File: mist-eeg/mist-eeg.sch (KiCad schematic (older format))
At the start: 3 parts

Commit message: Hooked-up the SoM
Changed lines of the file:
@@
 Wire Wire Line
 	2450 4200 2550 4200
-Text Label 1600 4200 2    50   ~ 0
-SD_DATA_DAT0
 Text Label 1600 4300 2    50   ~ 0
-SD_DATA_DAT1
+SD_DAT1
 Text Label 1600 4400 2    50   ~ 0
-SD_DATA_DAT2
+SD_DAT2
 Text Label 1600 4500 2    50   ~ 0
-SD_DATA_DAT3
+SD_DAT3
 Text Label 2550 4200 0    50   ~ 0
-SD_DATA_CMD
+SD_CMD
 Text Label 2550 4300 0    50   ~ 0
-SD_DATA_CLK
+SD_CLK
 Text Label 2550 4400 0    50   ~ 0
-SD_DATA_CONNECTED
+~SD_CONNECTED~
 $Sheet
 S 4250 1000 800  600
@@
 F7 "LRCLK" I R 5050 1200 50
 F8 "BCLK" I R 5050 1100 50
-F9 "PWR_OK" I R 5050 1450 50
+F9 "PWR_OK" I L 4250 1500 50
+F10 "MCLK" I R 5050 1400 50
 $EndSheet
 $Sheet
@@
 	4450 3700 4550 3700
 Text Label 4450 3400 2    50   ~ 0
-SD_DATA_DAT0
+SD_DAT0
 Text Label 4450 3500 2    50   ~ 0
-SD_DATA_DAT1
+SD_DAT1
 Text Label 4450 3600 2    50   ~ 0
-SD_DATA_DAT2
+SD_DAT2
 Text Label 4450 3700 2    50   ~ 0
-SD_DATA_DAT3
+SD_DAT3
 Wire Wire Line
 	4450 4000 4550 4000
@@
 	4550 3800 4450 3800
 Text Label 4450 3800 2    50   ~ 0
-SD_DATA_CMD
+SD_CMD
 Text Label 4450 3900 2    50   ~ 0
-SD_DATA_CLK
+SD_CLK
 Text Label 4450 4000 2    50   ~ 0
-SD_DATA_CONNECTED
+~SD_CONNECTED~
 Text Label 6500 3500 0    50   ~ 0
 USER1_G
@@
 Text Label 6500 4550 0    50   ~ 0
 USER
-Text Label 4500 4200 2    50   ~ 0
+Text Label 4500 4300 2    50   ~ 0
 ~EEG_CS~
-Text Label 4500 4300 2    50   ~ 0
+Text Label 4500 4400 2    50   ~ 0
 EEG_MOSI
-Text Label 4500 4400 2    50   ~ 0
+Text Label 4500 4500 2    50   ~ 0
 EEG_MISO
 Wire Wire Line
-	4500 4400 4550 4400
-Wire Wire Line
-	4550 4300 4500 4300
-Wire Wire Line
-	4500 4200 4550 4200
-Text Label 4500 4500 2    50   ~ 0
+	4500 4500 4550 4500
+Wire Wire Line
+	4550 4400 4500 4400
+Wire Wire Line
+	4500 4300 4550 4300
+Text Label 4500 4600 2    50   ~ 0
 EEG_SCK
 Wire Wire Line
-	4500 4500 4550 4500
-Wire Wire Line
 	4500 4600 4550 4600
-Text Label 4500 4600 2    50   ~ 0
+Wire Wire Line
+	4500 4700 4550 4700
+Text Label 4500 4700 2    50   ~ 0
 ~EEG_PWDN~
-Text Label 4500 4700 2    50   ~ 0
+Text Label 4500 4800 2    50   ~ 0
 ~EEG_RESET~
 Wire Wire Line
-	4500 4700 4550 4700
-Wire Wire Line
 	4500 4800 4550 4800
-Text Label 4500 4800 2    50   ~ 0
+Wire Wire Line
+	4500 4900 4550 4900
+Text Label 4500 4900 2    50   ~ 0
 EEG_START
-Text Label 4500 4900 2    50   ~ 0
+Text Label 4500 5000 2    50   ~ 0
 ~EEG_DRDY~
 Wire Wire Line
-	4500 4900 4550 4900
+	4500 5000 4550 5000
 Text Label 6500 4900 0    50   ~ 0
 AUDIO_BCLK
@@
 Text Label 1450 1250 2    50   ~ 0
 +5V0_ANA
-Text Label 4500 5100 2    50   ~ 0
+Text Label 4500 5150 2    50   ~ 0
 CTRL_SDA
-Text Label 4500 5200 2    50   ~ 0
+Text Label 4500 5250 2    50   ~ 0
 CTRL_SCL
 Wire Wire Line
-	4500 5200 4550 5200
-Wire Wire Line
-	4550 5100 4500 5100
+	4500 5250 4550 5250
+Wire Wire Line
+	4550 5150 4500 5150
 Text Label 2500 1350 0    50   ~ 0
 CTRL_SDA
@@
 Wire Wire Line
 	1450 1450 1500 1450
-Text Label 2550 4500 0    50   ~ 0
+Text Label 1600 4650 2    50   ~ 0
 +3V3_SD
 Wire Wire Line
-	2450 4500 2550 4500
+	1700 4650 1600 4650
 $Sheet
-S 1700 4150 750  450
+S 1700 4150 750  550
 U 60A0E6BC
 F0 "SD_DATA" 50
@@
 F6 "DAT0" B L 1700 4200 50
 F7 "DAT1" B L 1700 4300 50
-F8 "CON" O R 2450 4400 50
-F9 "+PWR_IN" I R 2450 4500 50
+F8 "~CD~" O R 2450 4400 50
+F9 "+PWR_IN" I L 1700 4650 50
+F10 "~RST~" I R 2450 4500 50
 $EndSheet
 Wire Wire Line
@@
 Wire Wire Line
 	2500 1550 2450 1550
-Text Label 4500 5350 2    50   ~ 0
+Text Label 4500 5400 2    50   ~ 0
 +5V_SOM
 Wire Wire Line
-	4500 5350 4550 5350
-Text Label 5100 1450 0    50   ~ 0
+	4500 5400 4550 5400
+Text Label 4200 1500 2    50   ~ 0
 AUDIO_PWR_OK
 Wire Wire Line
-	5100 1450 5050 1450
+	4200 1500 4250 1500
 $Sheet
 S 4550 3200 1900 2300
@@
 F0 "SoM" 50
 F1 "Coral-SoM.sch" 50
-F2 "SD_DATA_DAT0" B L 4550 3400 50
-F3 "SD_DATA_DAT1" B L 4550 3500 50
-F4 "SD_DATA_DAT2" B L 4550 3600 50
-F5 "SD_DATA_DAT3" B L 4550 3700 50
-F6 "SD_DATA_CMD" O L 4550 3800 50
-F7 "SD_DATA_CLK" O L 4550 3900 50
-F8 "SD_DATA_CONNECTED" I L 4550 4000 50
+F2 "SD_DAT0" B L 4550 3400 50
+F3 "SD_DAT1" B L 4550 3500 50
+F4 "SD_DAT2" B L 4550 3600 50
+F5 "SD_DAT3" B L 4550 3700 50
+F6 "SD_CMD" O L 4550 3800 50
+F7 "SD_CLK" O L 4550 3900 50
+F8 "~SD_CONNECTED~" I L 4550 4000 50
 F9 "USER1_R" O R 6450 3400 50
 F10 "USER1_G" O R 6450 3500 50
@@
 F19 "USER" I R 6450 4550 50
 F20 "START" I R 6450 4650 50
-F21 "~EEG_CS~" O L 4550 4200 50
-F22 "EEG_MOSI" O L 4550 4300 50
-F23 "EEG_MISO" I L 4550 4400 50
-F24 "EEG_SCK" O L 4550 4500 50
-F25 "~EEG_PWDN~" O L 4550 4600 50
-F26 "~EEG_RESET~" O L 4550 4700 50
-F27 "EEG_START" O L 4550 4800 50
-F28 "~EEG_DRDY~" I L 4550 4900 50
+F21 "~EEG_CS~" O L 4550 4300 50
+F22 "EEG_MOSI" O L 4550 4400 50
+F23 "EEG_MISO" I L 4550 4500 50
+F24 "EEG_SCK" O L 4550 4600 50
+F25 "~EEG_PWDN~" O L 4550 4700 50
+F26 "~EEG_RESET~" O L 4550 4800 50
+F27 "EEG_START" O L 4550 4900 50
+F28 "~EEG_DRDY~" I L 4550 5000 50
 F29 "AUDIO_BCLK" O R 6450 4900 50
 F30 "AUDIO_LRCLK" O R 6450 5000 50
@@
 F33 "AUDIO_SDA" B R 6450 5300 50
 F34 "AUDIO_SCL" O R 6450 5400 50
-F35 "CTRL_SDA" B L 4550 5100 50
-F36 "CTRL_SCL" O L 4550 5200 50
-F37 "+5V_SOM" I L 4550 5350 50
+F35 "CTRL_SDA" B L 4550 5150 50
+F36 "CTRL_SCL" O L 4550 5250 50
+F37 "+5V_SOM" I L 4550 5400 50
+F38 "+3V3_IN" I L 4550 3300 50
+F39 "AUDIO_MCLK" O R 6450 4800 50
+F40 "~SD_RST~" O L 4550 4100 50
 $EndSheet
+Text Label 5100 1400 0    50   ~ 0
+AUDIO_MCLK
+Wire Wire Line
+	5100 1400 5050 1400
+Text Label 6500 4800 0    50   ~ 0
+AUDIO_MCLK
+Wire Wire Line
+	6500 4800 6450 4800
+Text Label 4450 3300 2    50   ~ 0
++3V3_SD
+Wire Wire Line
+	4450 3300 4550 3300
+Text Label 1600 4200 2    50   ~ 0
+SD_DAT0
+Text Label 2550 4500 0    50   ~ 0
+~SD_RST~
+Wire Wire Line
+	4450 4100 4550 4100
+Text Label 4450 4100 2    50   ~ 0
+~SD_RST~
+Wire Wire Line
+	2450 4500 2550 4500
 $EndSCHEMATC

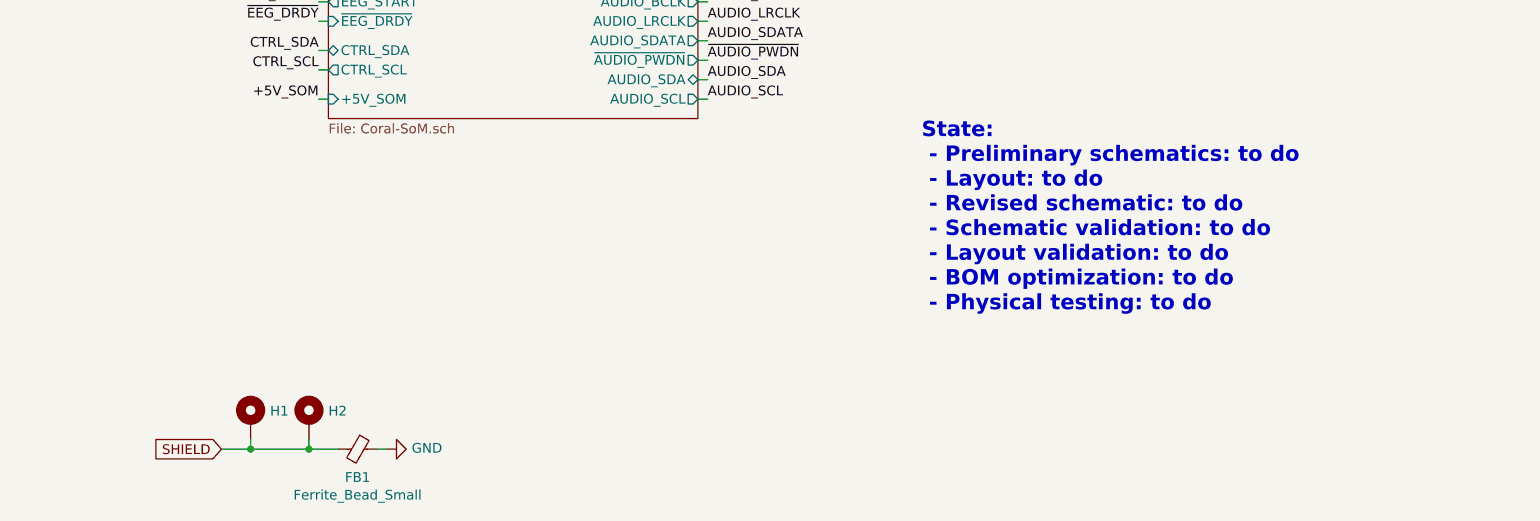
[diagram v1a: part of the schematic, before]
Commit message: Finish schematic and create interface specifications
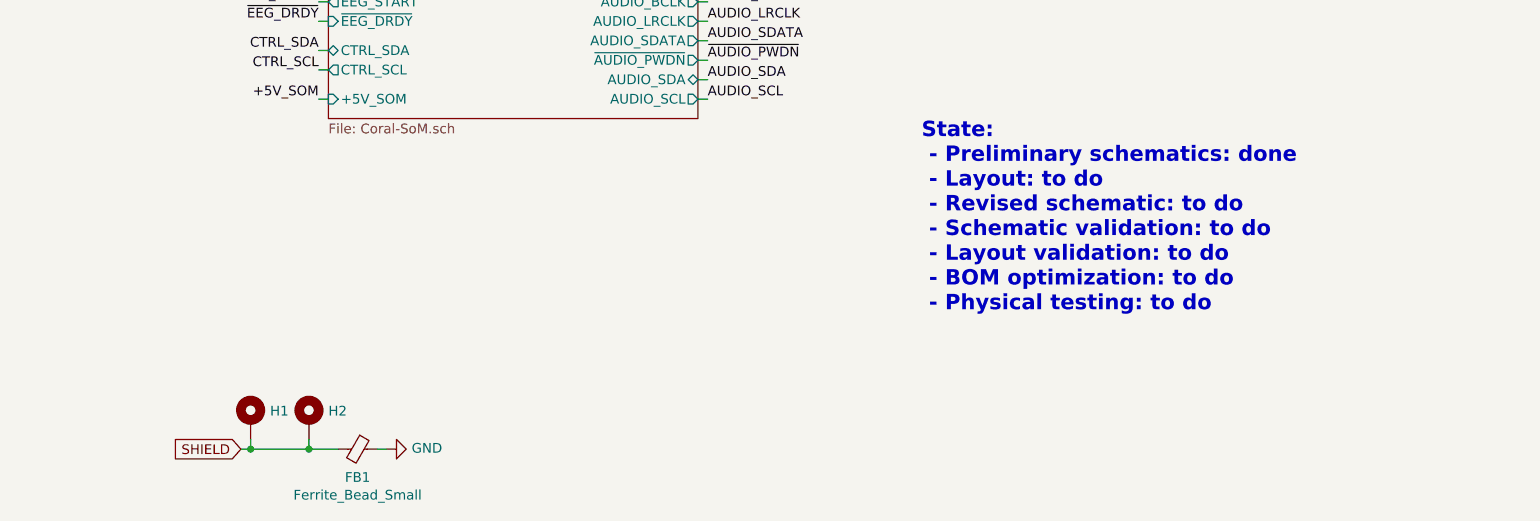
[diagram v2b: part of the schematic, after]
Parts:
- H1, H2: footprint MountingHole:MountingHole_2.7mm_M2.5_Pad -> mist-eeg:MountingHole_1.6mm
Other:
- note added: "State:\n - Preliminary schematics: done\n - Layout: to do\n - Revised schematic: to do\n - Schematic validation: to do\n - Layout validation: to do\n - BOM optimization: to do\n - Physical testing: to do"
- note removed: "State:\n - Preliminary schematics: to do\n - Layout: to do\n - Revised schematic: to do\n - Schematic validation: to do\n - Layout validation: to do\n - BOM optimization: to do\n - Physical testing: to do"
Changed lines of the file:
@@
 	2450 1250 2500 1250
 Text Notes 7600 6500 0    79   ~ 16
-State:\n - Preliminary schematics: to do\n - Layout: to do\n - Revised schematic: to do\n - Schematic validation: to do\n - Layout validation: to do\n - BOM optimization: to do\n - Physical testing: to do
+State:\n - Preliminary schematics: done\n - Layout: to do\n - Revised schematic: to do\n - Schematic validation: to do\n - Layout validation: to do\n - BOM optimization: to do\n - Physical testing: to do
 Text Notes 8900 1300 0    79   ~ 16
 PS I2C addresses:\n - 0x5C: HW monitor\n - 0x20: USB controller\n - 0x67: Clock fallback\n - 0x68: Clock
@@
 F 0 "H1" H 4250 7096 50  0000 L CNN
 F 1 "MountingHole" H 4250 7005 50  0001 L CNN
-F 2 "MountingHole:MountingHole_2.7mm_M2.5_Pad" H 4150 7050 50  0001 C CNN
+F 2 "mist-eeg:MountingHole_1.6mm" H 4150 7050 50  0001 C CNN
 F 3 "~" H 4150 7050 50  0001 C CNN
 	1    4150 7050
@@
 F 0 "H2" H 4550 7096 50  0000 L CNN
 F 1 "MountingHole" H 4550 7005 50  0001 L CNN
-F 2 "MountingHole:MountingHole_2.7mm_M2.5_Pad" H 4450 7050 50  0001 C CNN
+F 2 "mist-eeg:MountingHole_1.6mm" H 4450 7050 50  0001 C CNN
 F 3 "~" H 4450 7050 50  0001 C CNN
 	1    4450 7050
 	1    0    0    -1
 $EndComp
-Text GLabel 4000 7200 0    50   Input ~ 0
+Text GLabel 4100 7200 0    50   Input ~ 0
 SHIELD
 Wire Wire Line
@@
 Wire Wire Line
 	4450 7200 4600 7200
-Wire Wire Line
-	4000 7200 4150 7200
-Connection ~ 4150 7200
 Text Label 2500 1550 0    50   ~ 0
 +5V_SOM
@@
 Wire Wire Line
 	2450 4500 2550 4500
+Wire Wire Line
+	4100 7200 4150 7200
+Connection ~ 4150 7200
 $EndSCHEMATC

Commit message: Advance routing
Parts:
- removed FB1: Ferrite_Bead_Small, Resistor_SMD:R_0603_1608Metric, symbol Device:Ferrite_Bead_Small
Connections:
- net SHIELD: no longer names the net of H1.1
- net SHIELD: no longer H2.1
- no-connect marks 0 -> 2
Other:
- note added: "PS I2C addresses:\n - 0x5C: HW monitor"
- note removed: "PS I2C addresses:\n - 0x5C: HW monitor\n - 0x20: USB controller\n - 0x67: Clock fallback\n - 0x68: Clock"
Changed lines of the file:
@@
 $Descr USLetter 11000 8500
 encoding utf-8
-Sheet 1 12
+Sheet 1 11
 Title "Portiloop"
 Date "2021-06-07"
@@
 F0 "power" 50
 F1 "power.sch" 50
-F2 "+3V3" O L 1500 1450 50
+F2 "+3V3_SD" O L 1500 1450 50
 F3 "+5V0_ANA" O L 1500 1250 50
 F4 "+1V8_ANA" O L 1500 1350 50
@@
 State:\n - Preliminary schematics: done\n - Layout: to do\n - Revised schematic: to do\n - Schematic validation: to do\n - Layout validation: to do\n - BOM optimization: to do\n - Physical testing: to do
 Text Notes 8900 1300 0    79   ~ 16
-PS I2C addresses:\n - 0x5C: HW monitor\n - 0x20: USB controller\n - 0x67: Clock fallback\n - 0x68: Clock
+PS I2C addresses:\n - 0x5C: HW monitor
 $Comp
 L Mechanical:MountingHole_Pad H1
@@
 	1    0    0    -1
 $EndComp
-Text GLabel 4100 7200 0    50   Input ~ 0
-SHIELD
-Wire Wire Line
-	4450 7200 4450 7150
-Connection ~ 4450 7200
-Wire Wire Line
-	4150 7150 4150 7200
-Wire Wire Line
-	4150 7200 4450 7200
-$Comp
-L Device:Ferrite_Bead_Small FB?
-U 1 1 60D2C07C
-P 4700 7200
-AR Path="/609A79EB/60EAD252/60D2C07C" Ref="FB?"  Part="1"
-AR Path="/609A79EB/60BBE340/60D2C07C" Ref="FB?"  Part="1"
-AR Path="/60D2C07C" Ref="FB1"  Part="1"
-F 0 "FB1" V 4845 7200 50  0000 C CNN
-F 1 "Ferrite_Bead_Small" V 4936 7200 50  0000 C CNN
-F 2 "Resistor_SMD:R_0603_1608Metric" V 4630 7200 50  0001 C CNN
-F 3 "~" H 4700 7200 50  0001 C CNN
-	1    4700 7200
-	0    1    1    0
-$EndComp
-Wire Wire Line
-	4800 7200 4850 7200
 Text Label 2500 1450 0    50   ~ 0
 AUDIO_PWR_OK
 Wire Wire Line
 	2500 1450 2450 1450
-$Comp
-L power:GND #PWR01
-U 1 1 610A29B2
-P 4850 7200
-F 0 "#PWR01" H 4850 6950 50  0001 C CNN
-F 1 "GND" V 4855 7072 50  0000 R CNN
-F 2 "" H 4850 7200 50  0001 C CNN
-F 3 "" H 4850 7200 50  0001 C CNN
-	1    4850 7200
-	0    -1   -1   0
-$EndComp
 Text Label 1450 1450 2    50   ~ 0
 +3V3_SD
@@
 F10 "~RST~" I R 2450 4500 50
 $EndSheet
-Wire Wire Line
-	4450 7200 4600 7200
 Text Label 2500 1550 0    50   ~ 0
 +5V_SOM
@@
 Wire Wire Line
 	2450 4500 2550 4500
-Wire Wire Line
-	4100 7200 4150 7200
-Connection ~ 4150 7200
+NoConn ~ 4450 7150
+NoConn ~ 4150 7150
 $EndSCHEMATC

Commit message: Validation & fabrication layer
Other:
- note added: "State:\n - Preliminary schematics: done\n - Layout: done\n - Revised schematic: done\n - Schematic validation: done\n - Layout validation: done\n - BOM optimization: not done\n - Physical testing: to do"
- note removed: "State:\n - Preliminary schematics: done\n - Layout: to do\n - Revised schematic: to do\n - Schematic validation: to do\n - Layout validation: to do\n - BOM optimization: to do\n - Physical testing: to do"
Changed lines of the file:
@@
 	2450 1250 2500 1250
 Text Notes 7600 6500 0    79   ~ 16
-State:\n - Preliminary schematics: done\n - Layout: to do\n - Revised schematic: to do\n - Schematic validation: to do\n - Layout validation: to do\n - BOM optimization: to do\n - Physical testing: to do
+State:\n - Preliminary schematics: done\n - Layout: done\n - Revised schematic: done\n - Schematic validation: done\n - Layout validation: done\n - BOM optimization: not done\n - Physical testing: to do
 Text Notes 8900 1300 0    79   ~ 16
 PS I2C addresses:\n - 0x5C: HW monitor

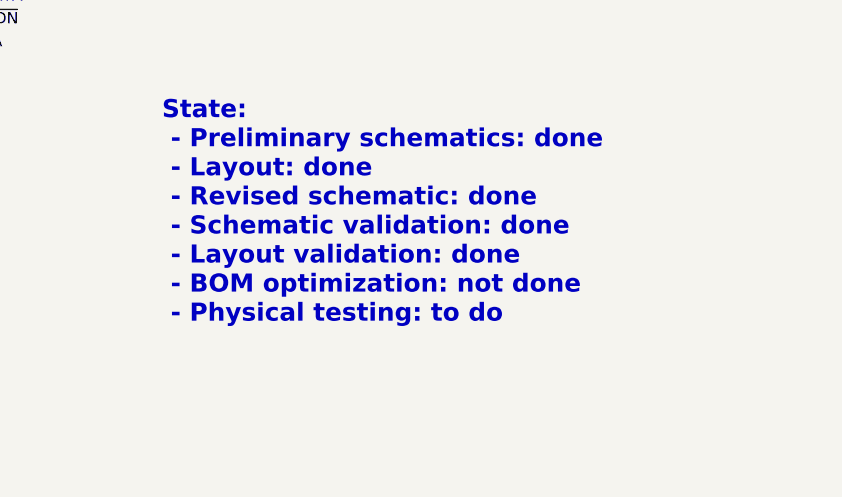
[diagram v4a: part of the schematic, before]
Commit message: Update footprints based upon piece availability & generate manufacturing files
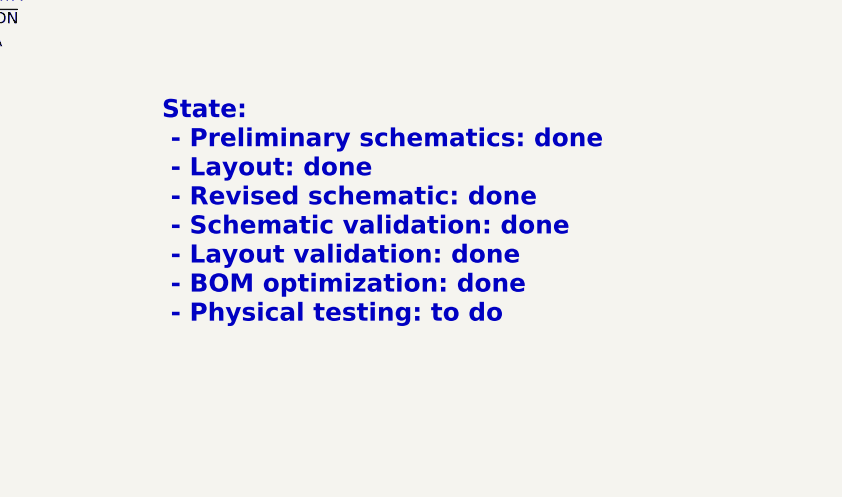
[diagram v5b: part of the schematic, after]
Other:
- note added: "State:\n - Preliminary schematics: done\n - Layout: done\n - Revised schematic: done\n - Schematic validation: done\n - Layout validation: done\n - BOM optimization: done\n - Physical testing: to do"
- note removed: "State:\n - Preliminary schematics: done\n - Layout: done\n - Revised schematic: done\n - Schematic validation: done\n - Layout validation: done\n - BOM optimization: not done\n - Physical testing: to do"
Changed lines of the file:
@@
 	2450 1250 2500 1250
 Text Notes 7600 6500 0    79   ~ 16
-State:\n - Preliminary schematics: done\n - Layout: done\n - Revised schematic: done\n - Schematic validation: done\n - Layout validation: done\n - BOM optimization: not done\n - Physical testing: to do
+State:\n - Preliminary schematics: done\n - Layout: done\n - Revised schematic: done\n - Schematic validation: done\n - Layout validation: done\n - BOM optimization: done\n - Physical testing: to do
 Text Notes 8900 1300 0    79   ~ 16
 PS I2C addresses:\n - 0x5C: HW monitor
